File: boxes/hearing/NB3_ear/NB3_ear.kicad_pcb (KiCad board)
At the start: 2 copper layers, 16 x 13 mm, 5 parts, among them J1 Conn_01x06_Male

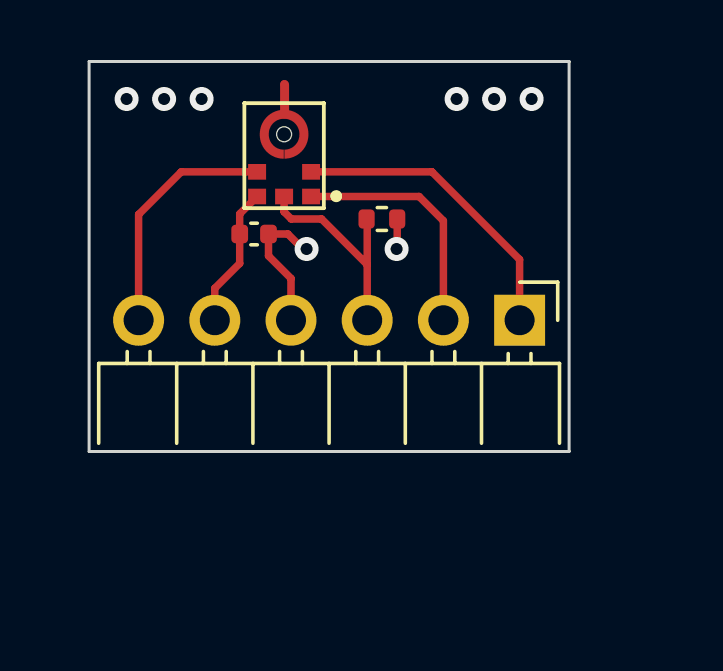
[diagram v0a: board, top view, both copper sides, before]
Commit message: Added NB3 Ear PCB design
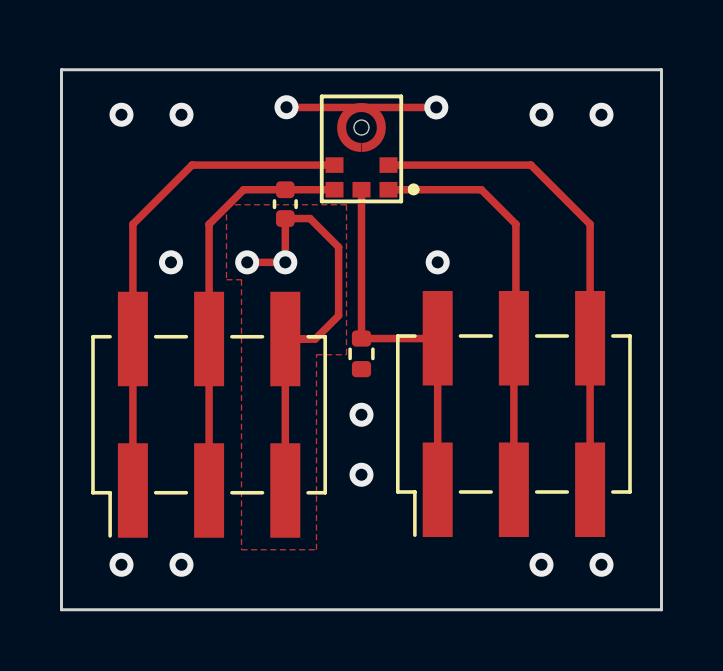
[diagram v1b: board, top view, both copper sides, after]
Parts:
- added J2: Conn_02x03_Odd_Even, Connector_PinHeader_2.54mm:PinHeader_2x03_P2.54mm_Vertical_SMD, F.Cu at (156.2, 109.8)
- J1: value Conn_01x06_Male -> Conn_02x03_Odd_Even; footprint Connector_PinHeader_2.54mm:PinHeader_1x06_P2.54mm_Horizontal -> Connector_PinHeader_2.54mm:PinHeader_2x03_P2.54mm_Vertical_SMD
- moved J1 10.8 mm to (146.0, 109.8), turned to 90 degrees
- moved G*** 7.34 mm to (151.1, 107.3)
- moved R1 4.55 mm to (151.1, 107.7), turned to 90 degrees
- moved MK1 2.59 mm to (151.1, 100.9)
- moved C1 1.44 mm to (148.5, 102.8), turned to -90 degrees
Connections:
- J1 pad 1: /LR -> /SCK
- J1 pad 2: /WS -> /SCK
- J1 pad 3: /SD -> +3V3
- J1 pad 4: GND -> +3V3
- J1 pad 5: +3V3 -> GND
- J1 pad 6: /SCK -> GND
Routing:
- net GND: track 6.68 -> 20.1 mm, vias 8 -> 16
- net +3V3: track 4.71 -> 13.5 mm
- net /SCK: track 8.06 -> 16.4 mm
- net /LR: track 10.2 -> 16.4 mm
- net /WS: track 8.06 -> 13.6 mm
- net /SD: track 7.40 -> 12.6 mm
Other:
- board size 16 x 13 mm -> 20 x 18 mm
